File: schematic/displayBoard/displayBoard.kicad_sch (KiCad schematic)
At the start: 30 parts, among them CON0 PINHD-1X10, IC1 4028D, T1 MMBTA42, T10 MMBTA42, T2 MMBTA42, T3 MMBTA42, T4 MMBTA42, T5 MMBTA42, T6 MMBTA42, T7 MMBTA42, T8 MMBTA42, T9 MMBTA42

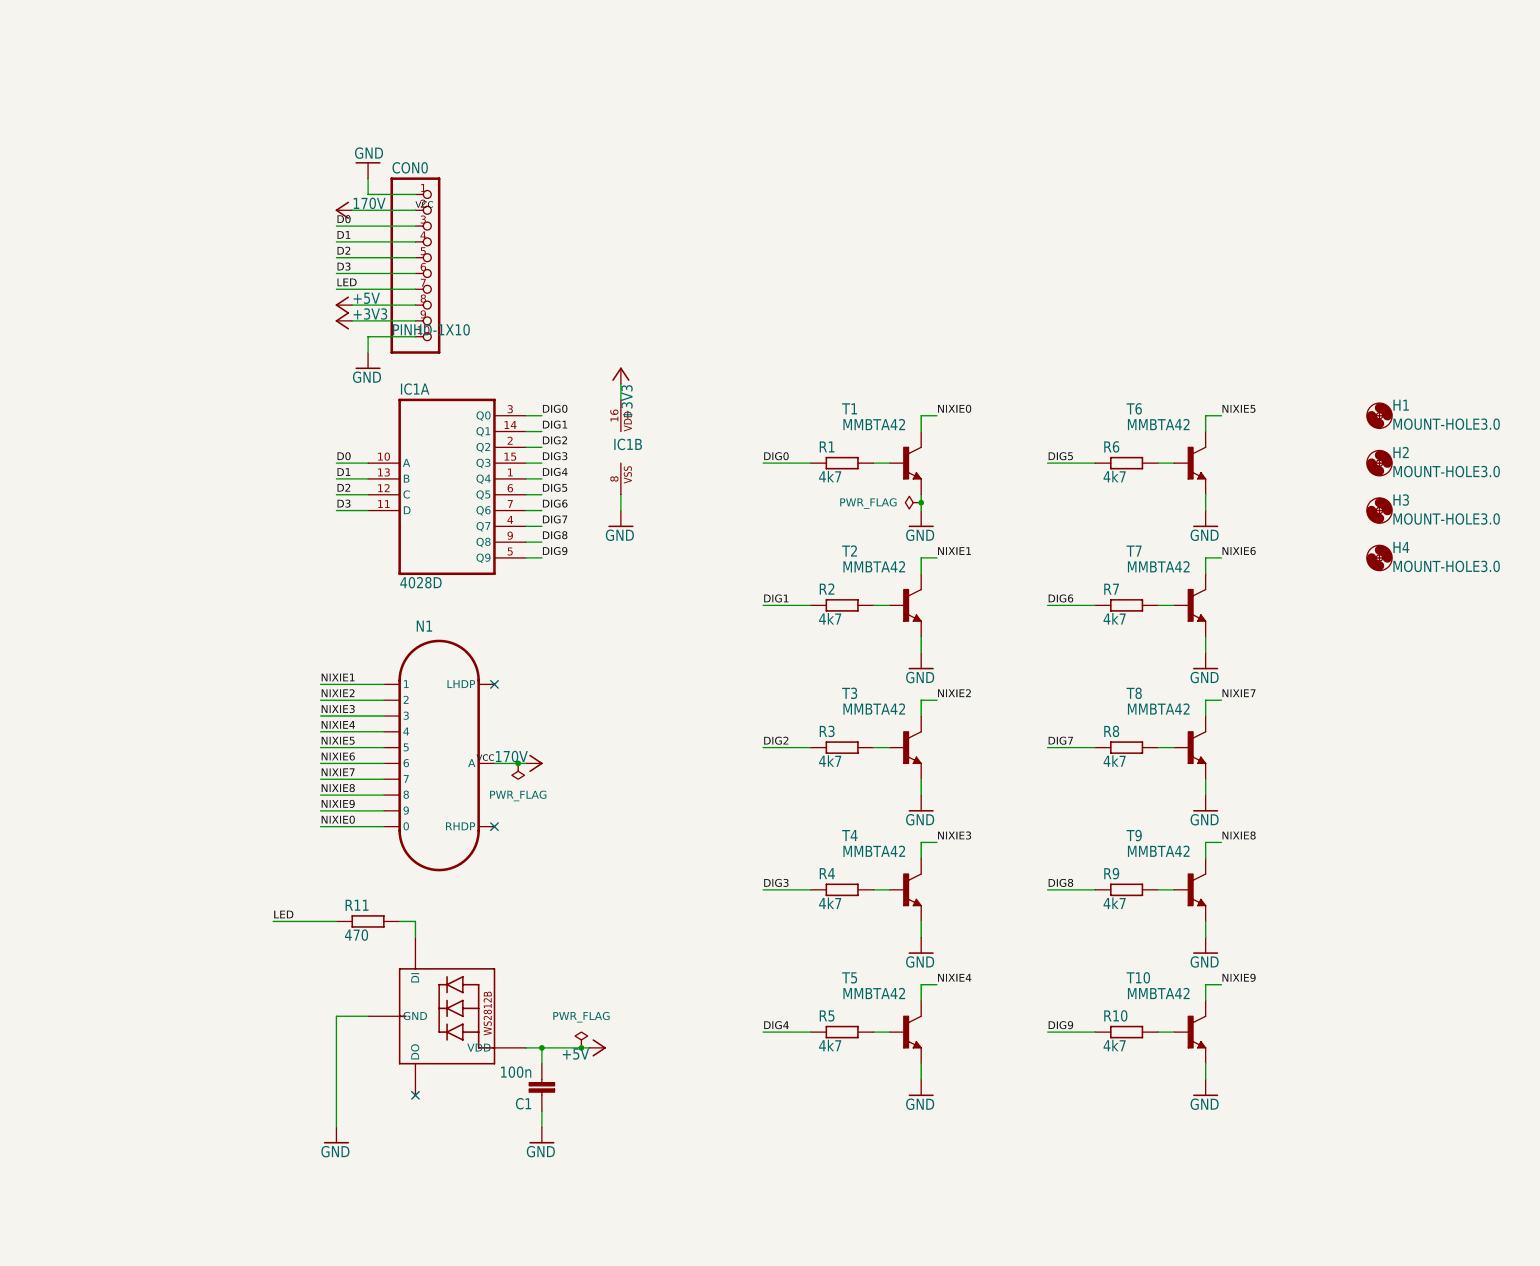
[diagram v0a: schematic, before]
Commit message: Re-wire control display with KiCad components
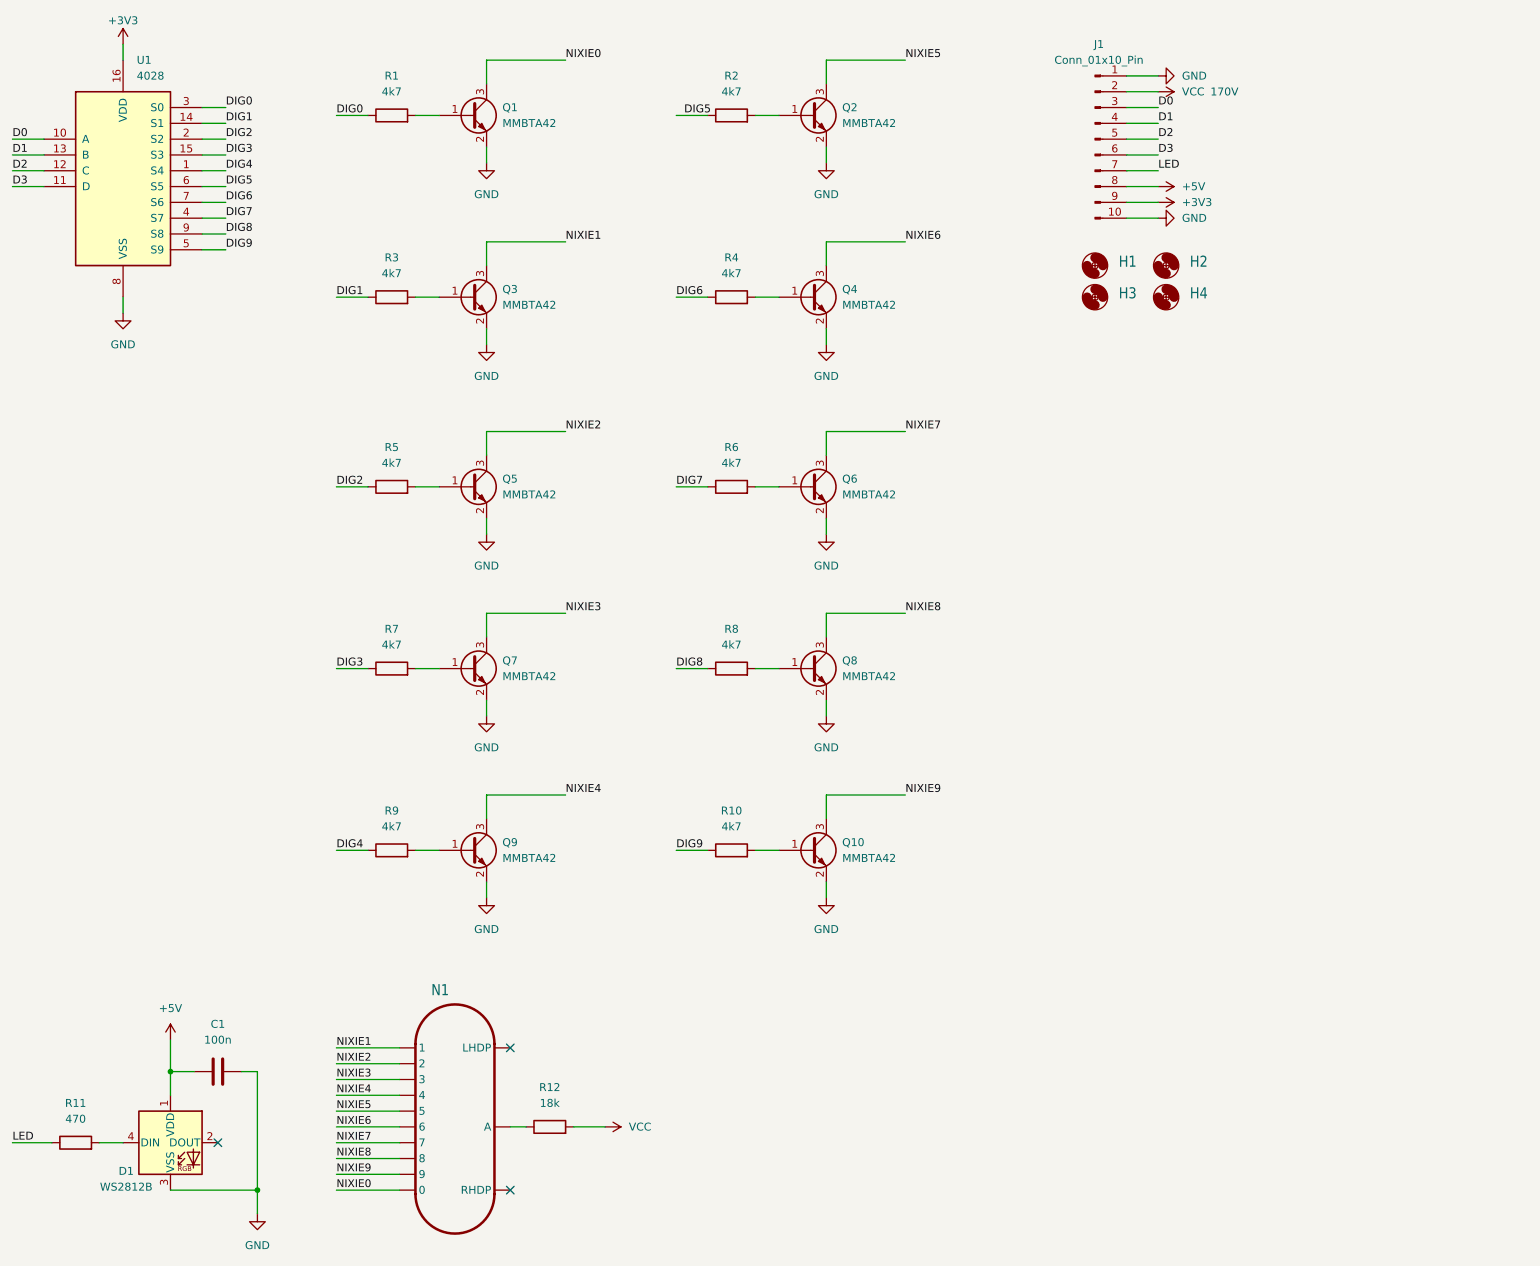
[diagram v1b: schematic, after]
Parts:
- removed C1: 100n, displayBoard:C0603, symbol displayBoard-eagle-import:C-EUC0603
- removed CON0: PINHD-1X10, displayBoard:1X10, symbol displayBoard-eagle-import:PINHD-1X10
- removed IC1: 4028D, displayBoard:SO16, symbol displayBoard-eagle-import:4028D
- removed LED1: WS2812B_5050N, displayBoard:WS2812B-NARROW, symbol displayBoard-eagle-import:WS2812B_5050N
- removed R1, R10, R2, R3, R4, R5, R6, R7, R8, R9: 4k7, displayBoard:R0603, symbol displayBoard-eagle-import:R-EU_R0603
- removed R11: 470, displayBoard:R0603, symbol displayBoard-eagle-import:R-EU_R0603
- removed T1, T10, T2, T3, T4, T5, T6, T7, T8, T9: MMBTA42, displayBoard:SOT23-BEC, symbol displayBoard-eagle-import:-NPN-SOT23-BEC
- added C1: 100n, Capacitor_SMD:C_0603_1608Metric, symbol Device:C
- added D1: WS2812B, LED_SMD:LED_WS2812B_PLCC4_5.0x5.0mm_P3.2mm, symbol LED:WS2812B
- added J1: Conn_01x10_Pin, Connector_PinHeader_2.54mm:PinHeader_1x10_P2.54mm_Vertical, symbol Connector:Conn_01x10_Pin
- added Q1, Q10, Q2, Q3, Q4, Q5, Q6, Q7, Q8, Q9: MMBTA42, Package_TO_SOT_SMD:SOT-23, symbol Transistor_BJT:MMBTA42
- added R1, R10, R2, R3, R4, R5, R6, R7, R8, R9: 4k7, Resistor_SMD:R_0603_1608Metric, symbol Device:R
- added R11: 470, Resistor_SMD:R_0603_1608Metric, symbol Device:R
- added R12: 18k, Resistor_SMD:R_0603_1608Metric, symbol Device:R
- added U1: 4028, Package_SO:SO-16_3.9x9.9mm_P1.27mm, symbol 4xxx:4028
- H1, H2, H3, H4: value MOUNT-HOLE3.0 -> ~; footprint displayBoard:3,0 -> MountingHole:MountingHole_3.2mm_M3
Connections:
- net +3V3: now also J1.9 (Pin_9), U1.16 (VDD)
- net +5V: now also C1.1, D1.1 (VDD), J1.8 (Pin_8)
- net D0: now also J1.3 (Pin_3), U1.10 (A)
- net D1: now also J1.4 (Pin_4), U1.13 (B)
- net D2: now also J1.5 (Pin_5), U1.12 (C)
- net D3: now also J1.6 (Pin_6), U1.11 (D)
- net DIG0: now also R1.1, U1.3 (S0)
- net DIG1: now also R3.1, U1.14 (S1)
- net DIG2: now also R5.1, U1.2 (S2)
- net DIG3: now also R7.1, U1.15 (S3)
- net DIG4: now also R9.1, U1.1 (S4)
- net DIG5: now also R2.1, U1.6 (S5)
- net DIG6: now also R4.1, U1.7 (S6)
- net DIG7: now also R6.1, U1.4 (S7)
- net DIG8: now also R8.1, U1.9 (S8)
- net DIG9: now also R10.1, U1.5 (S9)
- net GND: now also C1.2, D1.3 (VSS), J1.1 (Pin_1), J1.10 (Pin_10), Q1.2 (E), Q10.2 (E), Q2.2 (E), Q3.2 (E), Q4.2 (E), Q5.2 (E), Q6.2 (E), Q7.2 (E), Q8.2 (E), Q9.2 (E), U1.8 (VSS)
- net LED: now also J1.7 (Pin_7), R11.1
- net NIXIE0: now also Q1.3 (C)
- net NIXIE1: now also Q3.3 (C)
- net NIXIE2: now also Q5.3 (C)
- net NIXIE3: now also Q7.3 (C)
- net NIXIE4: now also Q9.3 (C)
- net NIXIE5: now also Q2.3 (C)
- net NIXIE6: now also Q4.3 (C)
- net NIXIE7: now also Q6.3 (C)
- net NIXIE8: now also Q8.3 (C)
- net NIXIE9: now also Q10.3 (C)
- net 170V: no longer names the net of N1.A
- net 170V: now also R12.1
- new net: Q8.1 (B), R8.2
- new net: Q7.1 (B), R7.2
- new net: Q2.1 (B), R2.2
- new net: Q3.1 (B), R3.2
- new net: Q5.1 (B), R5.2
- new net: D1.4 (DIN), R11.2
- new net: Q9.1 (B), R9.2
- new net: Q10.1 (B), R10.2
- new net: Q1.1 (B), R1.2
- new net: Q4.1 (B), R4.2
- new net: Q6.1 (B), R6.2
- new net VCC: J1.2 (Pin_2), R12.2
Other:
- note added: "170V"
- moved on the sheet: N1

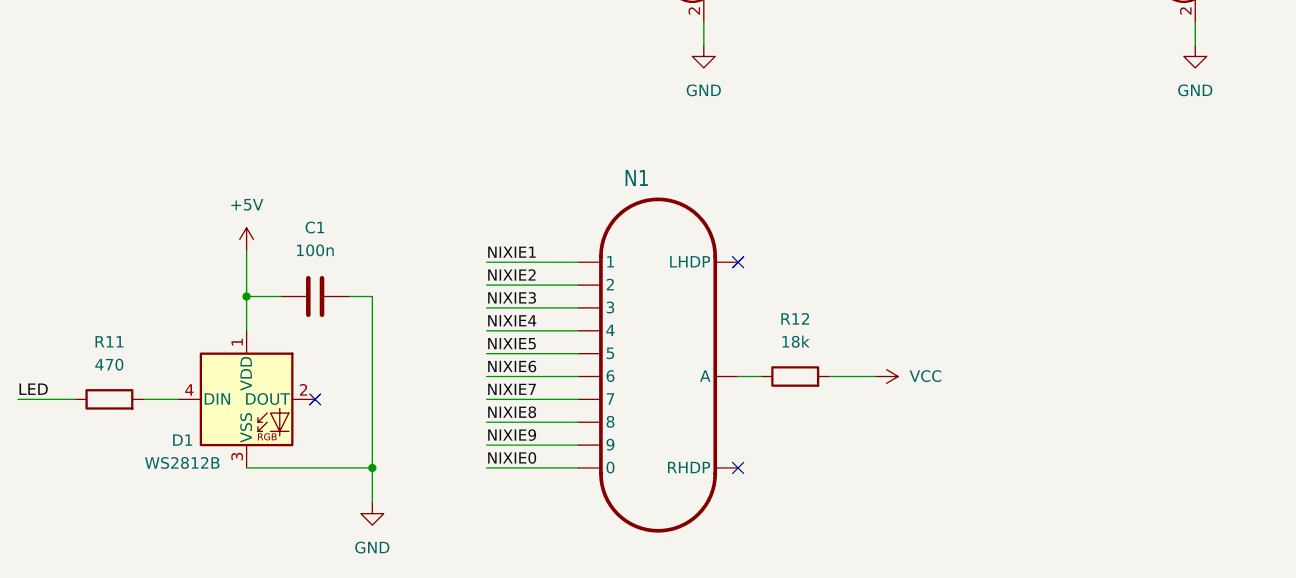
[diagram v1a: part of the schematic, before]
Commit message: Fix weird behaviour of the LED by adding a level shifter to DIN pin
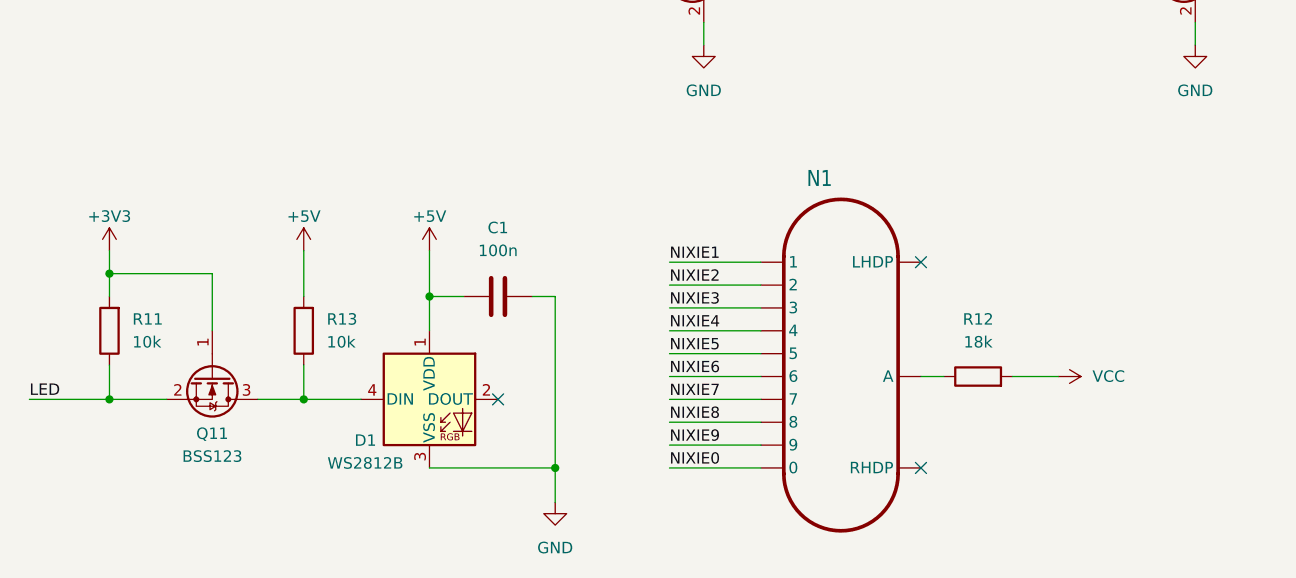
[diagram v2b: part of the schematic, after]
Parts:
- added Q11: BSS123, Package_TO_SOT_SMD:SOT-23, symbol Transistor_FET:BSS123
- added R13: 10k, Resistor_SMD:R_0603_1608Metric, symbol Device:R
- R11: value 470 -> 10k
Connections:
- net +3V3: now also R11.2, Q11.1 (G)
- net +5V: now also R13.2
- net LED: now also Q11.2 (S)
- net at D1.4 (DIN): now also Q11.3 (D), R13.1; no longer R11.2
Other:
- moved on the sheet: C1, D1, N1, R11, R12
